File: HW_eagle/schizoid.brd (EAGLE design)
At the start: 134 x 88.6 mm, 40 parts, among them IC1 628128, IC2 AT89S51-33P, IC3 74HC573N, IC4 4066N, IC5 74HC32N, IC6 74HC00N, IC7 74HCT257N, IC8 74HC00N, IC9 4066N, X2 PN61729-S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

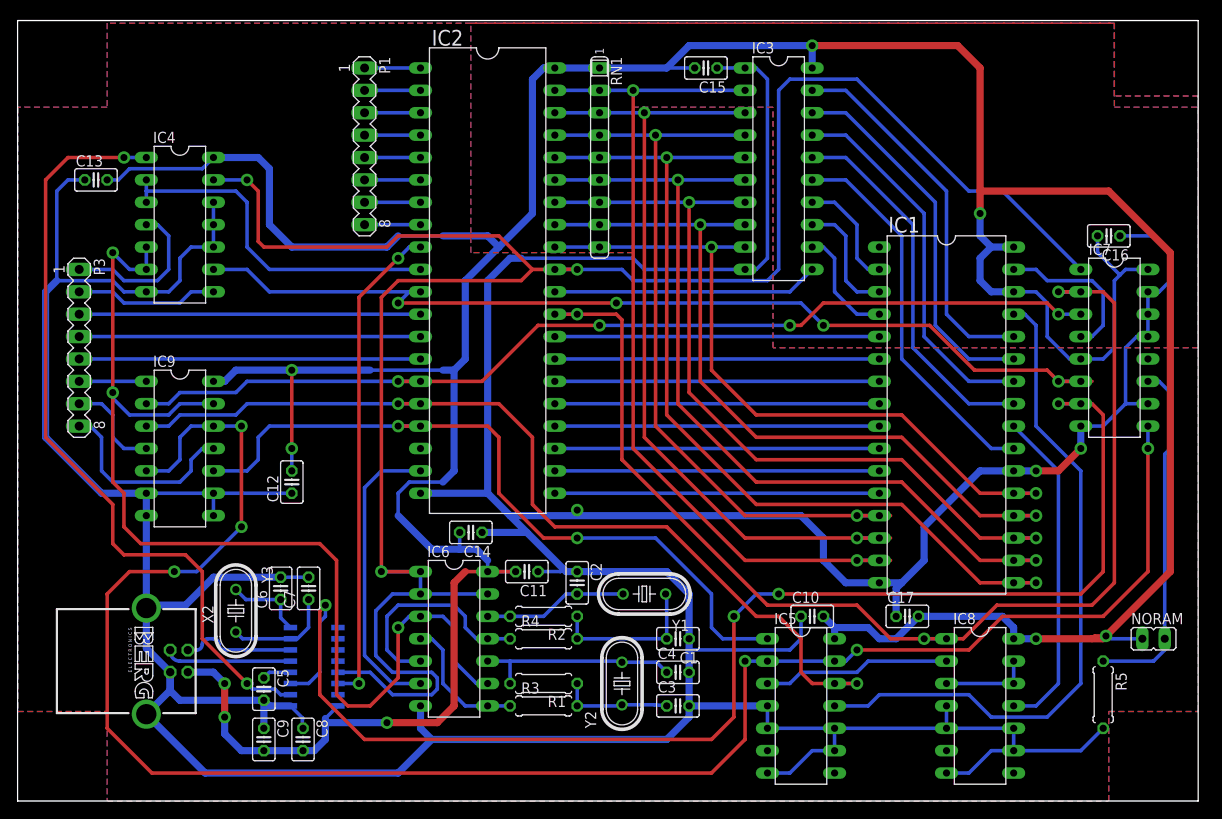
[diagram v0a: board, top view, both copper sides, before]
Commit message: Project was improved to contain all necessary information
Th comments in code were translated to English. BOM and part placement was added. Sources of terminal were found and thus added. README was changed.
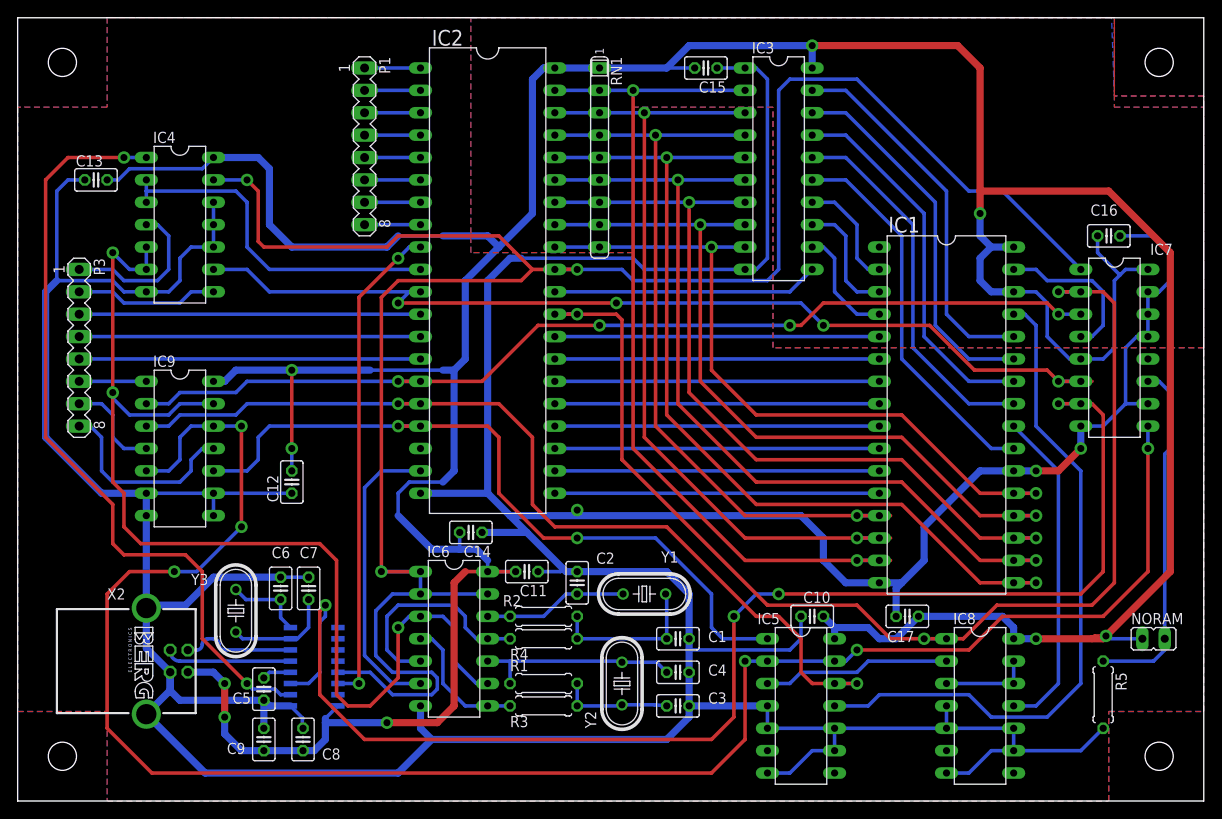
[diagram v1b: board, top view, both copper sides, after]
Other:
- board size 134 x 88.6 mm -> 134.6 x 88.9 mm
